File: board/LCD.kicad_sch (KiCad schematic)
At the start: 1 part

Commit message: LED Fix
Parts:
- LCD1: footprint NHD-0420H1Z-FL-GBW-33V3:LCD_NHD-0420H1Z-FL-GBW-33V3 -> LEDFootprint:LCD_NHD-0420H1Z-FL-GBW-33V3
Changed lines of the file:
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@@
 			)
 		)
-		(property "Footprint" "NHD-0420H1Z-FL-GBW-33V3:LCD_NHD-0420H1Z-FL-GBW-33V3"
+		(property "Footprint" "LEDFootprint:LCD_NHD-0420H1Z-FL-GBW-33V3"
 			(at 93.98 88.9 0)
 			(effects

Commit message: Finally assigned the footprints for current sensor, led, poe
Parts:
- LCD1: footprint LEDFootprint:LCD_NHD-0420H1Z-FL-GBW-33V3 -> PowerManagementBoard:LCD_NHD-0420H1Z-FL-GBW-33V3
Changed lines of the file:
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@@
 			)
 		)
-		(property "Footprint" "LEDFootprint:LCD_NHD-0420H1Z-FL-GBW-33V3"
+		(property "Footprint" "PowerManagementBoard:LCD_NHD-0420H1Z-FL-GBW-33V3"
 			(at 93.98 88.9 0)
 			(effects

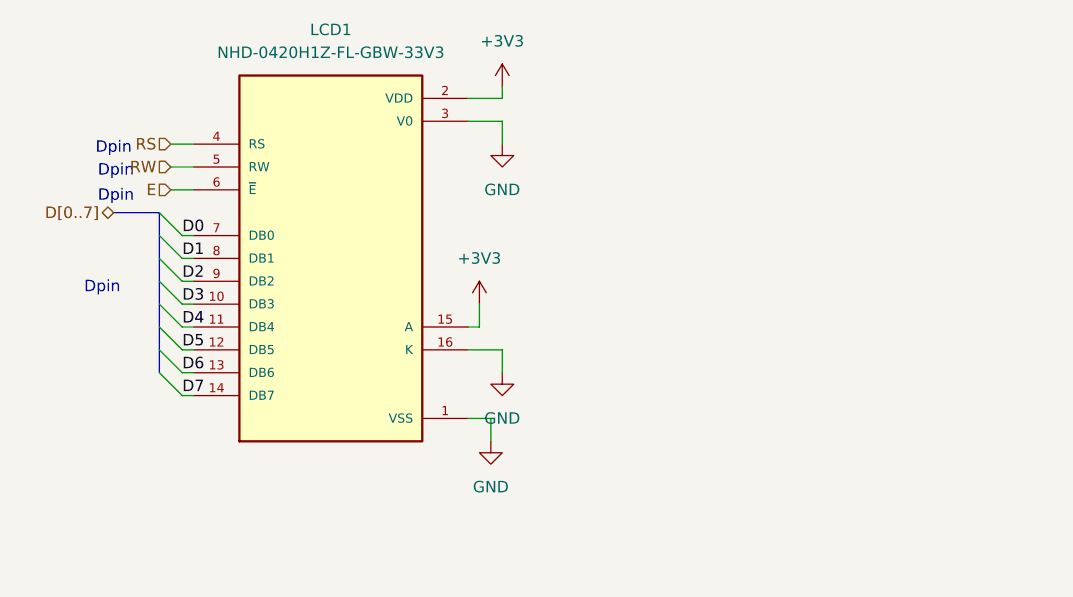
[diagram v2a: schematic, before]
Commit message: Center schematics and layout for prettiness
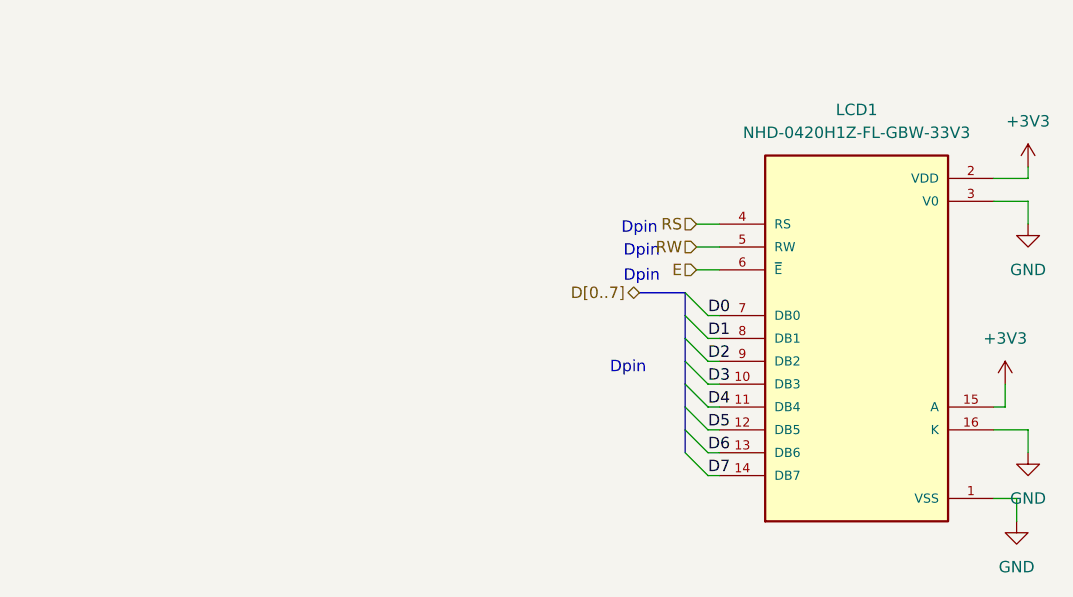
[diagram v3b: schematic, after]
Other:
- moved on the sheet: LCD1
